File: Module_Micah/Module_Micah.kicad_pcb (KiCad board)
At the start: 4 copper layers, 2 parts

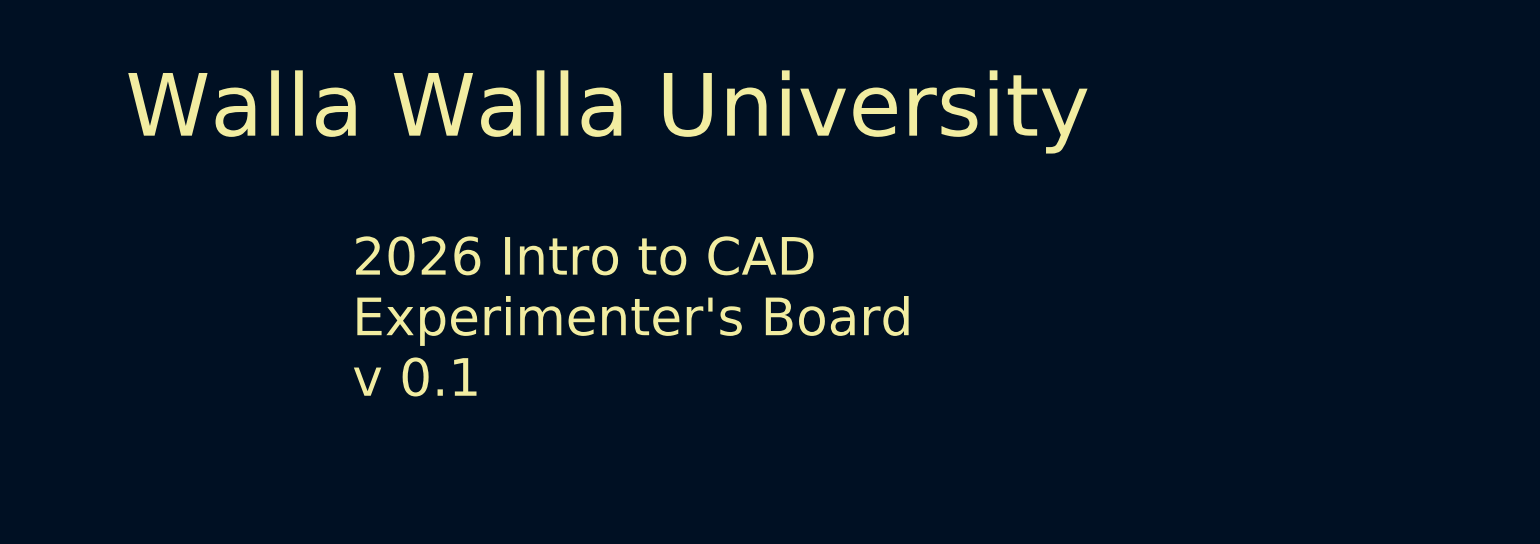
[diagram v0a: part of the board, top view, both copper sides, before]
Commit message: Modules iimporoted but not wired.
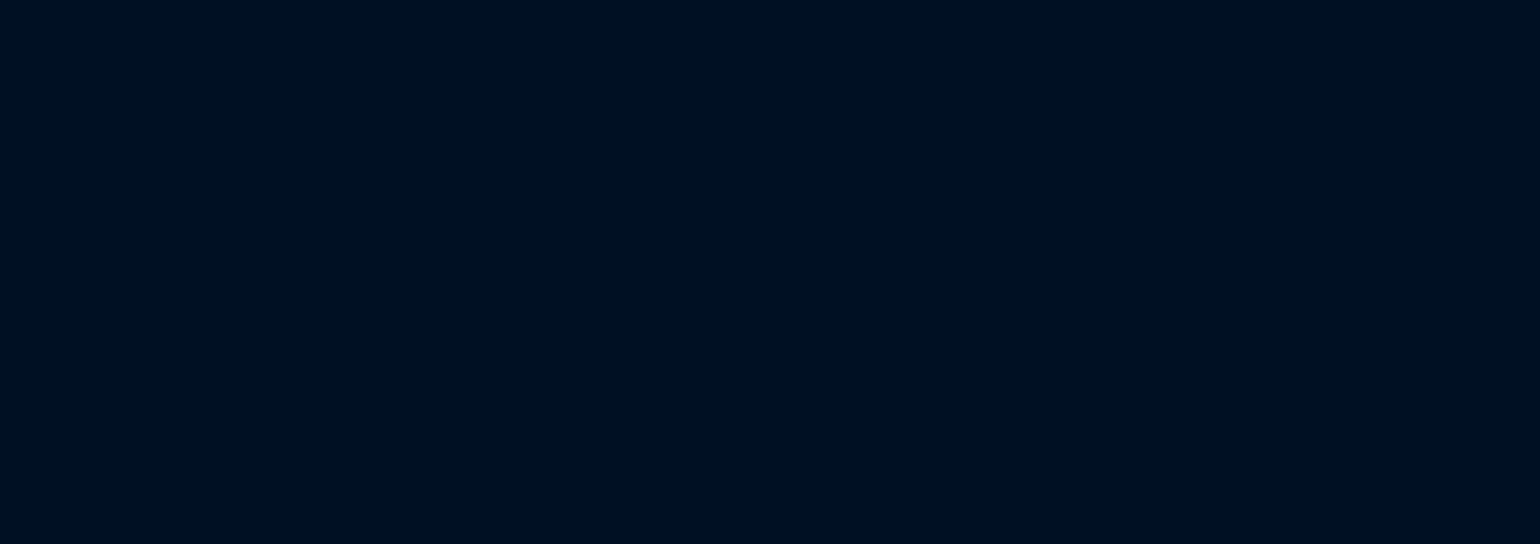
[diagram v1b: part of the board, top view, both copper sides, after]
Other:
- board text removed: "2026 Intro to CAD Experimenter's Board v 0.1"
- board text removed: "Walla Walla University"
